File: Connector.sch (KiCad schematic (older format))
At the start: 10 parts, among them CON11 DISCO-CON, CON12 DISCO-CON

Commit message: Resolves Bug in Cubesat Connector Library
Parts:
- removed CON12: DISCO-CON, cubesatFunkmodul:Cubesatconnector, symbol DISCO-CON
- CON11: footprint cubesatFunkmodul:Cubesatconnector -> CubeSat-Bus-1_FTS-CLP
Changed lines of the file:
@@
 $EndComp
 $Comp
-L GND #PWR035
+L GND #PWR37
 U 1 1 59C4523B
 P 2300 4700
-F 0 "#PWR035" H 2300 4450 50  0001 C CNN
+F 0 "#PWR37" H 2300 4450 50  0001 C CNN
 F 1 "GND" H 2300 4550 50  0000 C CNN
 F 2 "" H 2300 4700 50  0001 C CNN
@@
 $EndComp
 $Comp
-L GND #PWR036
+L GND #PWR38
 U 1 1 59C45255
 P 2600 4700
-F 0 "#PWR036" H 2600 4450 50  0001 C CNN
+F 0 "#PWR38" H 2600 4450 50  0001 C CNN
 F 1 "GND" H 2600 4550 50  0000 C CNN
 F 2 "" H 2600 4700 50  0001 C CNN
@@
 $EndComp
 $Comp
-L GND #PWR037
+L GND #PWR39
 U 1 1 59C4526F
 P 2900 4700
-F 0 "#PWR037" H 2900 4450 50  0001 C CNN
+F 0 "#PWR39" H 2900 4450 50  0001 C CNN
 F 1 "GND" H 2900 4550 50  0000 C CNN
 F 2 "" H 2900 4700 50  0001 C CNN
@@
 $EndComp
 $Comp
-L GND #PWR038
+L GND #PWR40
 U 1 1 59C452E4
 P 3400 4700
-F 0 "#PWR038" H 3400 4450 50  0001 C CNN
+F 0 "#PWR40" H 3400 4450 50  0001 C CNN
 F 1 "GND" H 3400 4550 50  0000 C CNN
 F 2 "" H 3400 4700 50  0001 C CNN
@@
 $EndComp
 $Comp
-L GND #PWR039
+L GND #PWR43
 U 1 1 59C452EA
 P 3700 4700
-F 0 "#PWR039" H 3700 4450 50  0001 C CNN
+F 0 "#PWR43" H 3700 4450 50  0001 C CNN
 F 1 "GND" H 3700 4550 50  0000 C CNN
 F 2 "" H 3700 4700 50  0001 C CNN
@@
 $EndComp
 $Comp
-L GND #PWR040
+L GND #PWR44
 U 1 1 59C452F0
 P 4000 4700
-F 0 "#PWR040" H 4000 4450 50  0001 C CNN
+F 0 "#PWR44" H 4000 4450 50  0001 C CNN
 F 1 "GND" H 4000 4550 50  0000 C CNN
 F 2 "" H 4000 4700 50  0001 C CNN
@@
 $EndComp
 $Comp
-L GND #PWR041
+L GND #PWR45
 U 1 1 59C45994
 P 4650 4700
-F 0 "#PWR041" H 4650 4450 50  0001 C CNN
+F 0 "#PWR45" H 4650 4450 50  0001 C CNN
 F 1 "GND" H 4650 4550 50  0000 C CNN
 F 2 "" H 4650 4700 50  0001 C CNN
@@
 ESD Protection
 $Comp
-L GND #PWR042
-U 1 1 59DA7E4B
-P 7550 950
-F 0 "#PWR042" H 7550 700 50  0001 C CNN
-F 1 "GND" H 7550 800 50  0000 C CNN
-F 2 "" H 7550 950 50  0001 C CNN
-F 3 "" H 7550 950 50  0001 C CNN
-	1    7550 950
-	0    -1   -1   0
-$EndComp
-$Comp
-L GND #PWR043
+L GND #PWR47
 U 1 1 59DA7E71
-P 6250 1200
-F 0 "#PWR043" H 6250 950 50  0001 C CNN
-F 1 "GND" H 6250 1050 50  0000 C CNN
-F 2 "" H 6250 1200 50  0001 C CNN
-F 3 "" H 6250 1200 50  0001 C CNN
-	1    6250 1200
-	0    1    1    0
-$EndComp
-$Comp
-L GND #PWR044
+P 7100 1400
+F 0 "#PWR47" H 7100 1150 50  0001 C CNN
+F 1 "GND" H 7100 1250 50  0000 C CNN
+F 2 "" H 7100 1400 50  0001 C CNN
+F 3 "" H 7100 1400 50  0001 C CNN
+	1    7100 1400
+	0    -1   -1   0
+$EndComp
+$Comp
+L GND #PWR48
 U 1 1 59DA7F27
-P 6250 3100
-F 0 "#PWR044" H 6250 2850 50  0001 C CNN
-F 1 "GND" H 6250 2950 50  0000 C CNN
-F 2 "" H 6250 3100 50  0001 C CNN
-F 3 "" H 6250 3100 50  0001 C CNN
-	1    6250 3100
-	0    1    1    0
-$EndComp
-$Comp
-L GND #PWR045
-U 1 1 59DA7F4D
-P 7550 3850
-F 0 "#PWR045" H 7550 3600 50  0001 C CNN
-F 1 "GND" H 7550 3700 50  0000 C CNN
-F 2 "" H 7550 3850 50  0001 C CNN
-F 3 "" H 7550 3850 50  0001 C CNN
-	1    7550 3850
-	0    -1   -1   0
-$EndComp
-$Comp
-L GND #PWR046
+P 7100 4300
+F 0 "#PWR48" H 7100 4050 50  0001 C CNN
+F 1 "GND" H 7100 4150 50  0000 C CNN
+F 2 "" H 7100 4300 50  0001 C CNN
+F 3 "" H 7100 4300 50  0001 C CNN
+	1    7100 4300
+	0    -1   -1   0
+$EndComp
+$Comp
+L GND #PWR41
 U 1 1 59DA801E
 P 3600 1200
-F 0 "#PWR046" H 3600 950 50  0001 C CNN
+F 0 "#PWR41" H 3600 950 50  0001 C CNN
 F 1 "GND" H 3600 1050 50  0000 C CNN
 F 2 "" H 3600 1200 50  0001 C CNN
@@
 $EndComp
 $Comp
-L GND #PWR047
+L GND #PWR35
 U 1 1 59DA8044
 P 2000 1200
-F 0 "#PWR047" H 2000 950 50  0001 C CNN
+F 0 "#PWR35" H 2000 950 50  0001 C CNN
 F 1 "GND" H 2000 1050 50  0000 C CNN
 F 2 "" H 2000 1200 50  0001 C CNN
@@
 $EndComp
 $Comp
-L GND #PWR048
+L GND #PWR36
 U 1 1 59DA8115
 P 2000 3100
-F 0 "#PWR048" H 2000 2850 50  0001 C CNN
+F 0 "#PWR36" H 2000 2850 50  0001 C CNN
 F 1 "GND" H 2000 2950 50  0000 C CNN
 F 2 "" H 2000 3100 50  0001 C CNN
@@
 $EndComp
 $Comp
-L GND #PWR049
+L GND #PWR42
 U 1 1 59DA82BE
 P 3600 3100
-F 0 "#PWR049" H 3600 2850 50  0001 C CNN
+F 0 "#PWR42" H 3600 2850 50  0001 C CNN
 F 1 "GND" H 3600 2950 50  0000 C CNN
 F 2 "" H 3600 3100 50  0001 C CNN
@@
 $EndComp
 $Comp
-L GND #PWR050
+L GND #PWR46
 U 1 1 59DAB906
 P 5100 4650
-F 0 "#PWR050" H 5100 4400 50  0001 C CNN
+F 0 "#PWR46" H 5100 4400 50  0001 C CNN
 F 1 "GND" H 5100 4500 50  0000 C CNN
 F 2 "" H 5100 4650 50  0001 C CNN
@@
 $EndComp
 $Comp
-L DISCO-CON CON12
-U 1 1 59E5D7B1
-P 10400 2250
-F 0 "CON12" H 10100 3780 45  0000 L BNN
-F 1 "DISCO-CON" H 10100 570 45  0000 L BNN
-F 2 "cubesatFunkmodul:Cubesatconnector" H 10430 2400 20  0001 C CNN
-F 3 "" H 10400 2250 60  0001 C CNN
-	1    10400 2250
-	1    0    0    -1
-$EndComp
-$Comp
 L DISCO-CON CON11
-U 1 1 59E5D88F
-P 7050 2350
-F 0 "CON11" H 6750 3880 45  0000 L BNN
-F 1 "DISCO-CON" H 6750 670 45  0000 L BNN
-F 2 "cubesatFunkmodul:Cubesatconnector" H 7080 2500 20  0001 C CNN
-F 3 "" H 7050 2350 60  0001 C CNN
-	1    7050 2350
+U 1 1 59F62198
+P 6600 2800
+F 0 "CON11" H 6300 4330 45  0000 L BNN
+F 1 "DISCO-CON" H 6300 1120 45  0000 L BNN
+F 2 "CubeSat-Bus-1_FTS-CLP" H 6630 2950 20  0001 C CNN
+F 3 "" H 6600 2800 60  0001 C CNN
+	1    6600 2800
 	-1   0    0    -1
 $EndComp

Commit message: Integrates Connectors in Design
Beginn to add mounting holes
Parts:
- removed CON11: DISCO-CON, CubeSat-Bus-1_FTS-CLP, symbol DISCO-CON
- added CON11: DISCO-CON1, cubesatFunkmodul:Cubesatconnector, symbol DISCO-CON1
- added CON21: DISCO-CON2, cubesatFunkmodul:Cubesatconnector, symbol DISCO-CON2
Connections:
- net labels added: TCK, TDI, TDO, TDO-Rf, TMS, ~RBF~
- net labels removed: VBAT
- wire segments 4 -> 1
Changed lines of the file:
@@
 LIBS:nxp-ic
 LIBS:7400-ic
-LIBS:cubesatFunkmodul-cache
 LIBS:funkmodul
 LIBS:CubeSat-Bus-1
 LIBS:CubeSat-Bus-2
+LIBS:disco-con
 EELAYER 25 0
 EELAYER END
@@
 $EndComp
 $Comp
-L GND #PWR37
+L GND #PWR035
 U 1 1 59C4523B
 P 2300 4700
-F 0 "#PWR37" H 2300 4450 50  0001 C CNN
+F 0 "#PWR035" H 2300 4450 50  0001 C CNN
 F 1 "GND" H 2300 4550 50  0000 C CNN
 F 2 "" H 2300 4700 50  0001 C CNN
@@
 $EndComp
 $Comp
-L GND #PWR38
+L GND #PWR036
 U 1 1 59C45255
 P 2600 4700
-F 0 "#PWR38" H 2600 4450 50  0001 C CNN
+F 0 "#PWR036" H 2600 4450 50  0001 C CNN
 F 1 "GND" H 2600 4550 50  0000 C CNN
 F 2 "" H 2600 4700 50  0001 C CNN
@@
 $EndComp
 $Comp
-L GND #PWR39
+L GND #PWR037
 U 1 1 59C4526F
 P 2900 4700
-F 0 "#PWR39" H 2900 4450 50  0001 C CNN
+F 0 "#PWR037" H 2900 4450 50  0001 C CNN
 F 1 "GND" H 2900 4550 50  0000 C CNN
 F 2 "" H 2900 4700 50  0001 C CNN
@@
 $EndComp
 $Comp
-L GND #PWR40
+L GND #PWR038
 U 1 1 59C452E4
 P 3400 4700
-F 0 "#PWR40" H 3400 4450 50  0001 C CNN
+F 0 "#PWR038" H 3400 4450 50  0001 C CNN
 F 1 "GND" H 3400 4550 50  0000 C CNN
 F 2 "" H 3400 4700 50  0001 C CNN
@@
 $EndComp
 $Comp
-L GND #PWR43
+L GND #PWR039
 U 1 1 59C452EA
 P 3700 4700
-F 0 "#PWR43" H 3700 4450 50  0001 C CNN
+F 0 "#PWR039" H 3700 4450 50  0001 C CNN
 F 1 "GND" H 3700 4550 50  0000 C CNN
 F 2 "" H 3700 4700 50  0001 C CNN
@@
 $EndComp
 $Comp
-L GND #PWR44
+L GND #PWR040
 U 1 1 59C452F0
 P 4000 4700
-F 0 "#PWR44" H 4000 4450 50  0001 C CNN
+F 0 "#PWR040" H 4000 4450 50  0001 C CNN
 F 1 "GND" H 4000 4550 50  0000 C CNN
 F 2 "" H 4000 4700 50  0001 C CNN
@@
 $EndComp
 $Comp
-L GND #PWR45
+L GND #PWR041
 U 1 1 59C45994
 P 4650 4700
-F 0 "#PWR45" H 4650 4450 50  0001 C CNN
+F 0 "#PWR041" H 4650 4450 50  0001 C CNN
 F 1 "GND" H 4650 4550 50  0000 C CNN
 F 2 "" H 4650 4700 50  0001 C CNN
@@
 ESD Protection
 $Comp
-L GND #PWR47
+L GND #PWR042
 U 1 1 59DA7E71
 P 7100 1400
-F 0 "#PWR47" H 7100 1150 50  0001 C CNN
+F 0 "#PWR042" H 7100 1150 50  0001 C CNN
 F 1 "GND" H 7100 1250 50  0000 C CNN
 F 2 "" H 7100 1400 50  0001 C CNN
@@
 $EndComp
 $Comp
-L GND #PWR48
+L GND #PWR043
 U 1 1 59DA7F27
 P 7100 4300
-F 0 "#PWR48" H 7100 4050 50  0001 C CNN
+F 0 "#PWR043" H 7100 4050 50  0001 C CNN
 F 1 "GND" H 7100 4150 50  0000 C CNN
 F 2 "" H 7100 4300 50  0001 C CNN
@@
 	0    -1   -1   0
 $EndComp
-$Comp
-L GND #PWR41
-U 1 1 59DA801E
-P 3600 1200
-F 0 "#PWR41" H 3600 950 50  0001 C CNN
-F 1 "GND" H 3600 1050 50  0000 C CNN
-F 2 "" H 3600 1200 50  0001 C CNN
-F 3 "" H 3600 1200 50  0001 C CNN
-	1    3600 1200
-	0    -1   -1   0
-$EndComp
-$Comp
-L GND #PWR35
-U 1 1 59DA8044
-P 2000 1200
-F 0 "#PWR35" H 2000 950 50  0001 C CNN
-F 1 "GND" H 2000 1050 50  0000 C CNN
-F 2 "" H 2000 1200 50  0001 C CNN
-F 3 "" H 2000 1200 50  0001 C CNN
-	1    2000 1200
-	0    1    1    0
-$EndComp
-$Comp
-L GND #PWR36
-U 1 1 59DA8115
-P 2000 3100
-F 0 "#PWR36" H 2000 2850 50  0001 C CNN
-F 1 "GND" H 2000 2950 50  0000 C CNN
-F 2 "" H 2000 3100 50  0001 C CNN
-F 3 "" H 2000 3100 50  0001 C CNN
-	1    2000 3100
-	0    1    1    0
-$EndComp
-$Comp
-L GND #PWR42
-U 1 1 59DA82BE
-P 3600 3100
-F 0 "#PWR42" H 3600 2850 50  0001 C CNN
-F 1 "GND" H 3600 2950 50  0000 C CNN
-F 2 "" H 3600 3100 50  0001 C CNN
-F 3 "" H 3600 3100 50  0001 C CNN
-	1    3600 3100
-	0    -1   -1   0
-$EndComp
-Text HLabel 1650 1400 0    60   Input ~ 0
+Text HLabel 7100 2100 2    60   Input ~ 0
 3.3V
-Text HLabel 3850 1400 2    60   Input ~ 0
-3.3V
-Wire Wire Line
-	1650 1400 2000 1400
-Wire Wire Line
-	3600 1400 3850 1400
-Text GLabel 1650 1300 0    60   Input ~ 0
-VBAT
-Text GLabel 3900 1300 2    60   Input ~ 0
-VBAT
-Wire Wire Line
-	3600 1300 3900 1300
-Wire Wire Line
-	1650 1300 2000 1300
-Text HLabel 6250 2200 0    60   Input ~ 0
+Text HLabel 7100 3500 2    60   Input ~ 0
 TX1
-Text HLabel 6250 2300 0    60   Input ~ 0
+Text HLabel 7100 3600 2    60   Input ~ 0
 RX1
-Text HLabel 7850 2200 2    60   Input ~ 0
+Text HLabel 9450 2900 0    60   Input ~ 0
 TX2
-Text HLabel 7850 2300 2    60   Input ~ 0
+Text HLabel 9450 2800 0    60   Input ~ 0
 RX2
-Text HLabel 6250 1900 0    60   Input ~ 0
-BAT_OK
-Text HLabel 7850 1900 2    60   Input ~ 0
-BAT_OK
 Text HLabel 5100 4350 1    60   Input ~ 0
 BAT_OK
@@
 $EndComp
 $Comp
-L GND #PWR46
+L GND #PWR044
 U 1 1 59DAB906
 P 5100 4650
-F 0 "#PWR46" H 5100 4400 50  0001 C CNN
+F 0 "#PWR044" H 5100 4400 50  0001 C CNN
 F 1 "GND" H 5100 4500 50  0000 C CNN
 F 2 "" H 5100 4650 50  0001 C CNN
@@
 $EndComp
 $Comp
-L DISCO-CON CON11
-U 1 1 59F62198
+L DISCO-CON2 CON21
+U 1 1 59FBB064
+P 9950 2700
+F 0 "CON21" H 9650 4230 45  0000 L BNN
+F 1 "DISCO-CON2" H 9650 1020 45  0000 L BNN
+F 2 "cubesatFunkmodul:Cubesatconnector" H 9980 2850 20  0001 C CNN
+F 3 "" H 9950 2700 60  0001 C CNN
+	1    9950 2700
+	1    0    0    -1
+$EndComp
+$Comp
+L DISCO-CON1 CON11
+U 1 1 59FBB0E1
 P 6600 2800
 F 0 "CON11" H 6300 4330 45  0000 L BNN
-F 1 "DISCO-CON" H 6300 1120 45  0000 L BNN
-F 2 "CubeSat-Bus-1_FTS-CLP" H 6630 2950 20  0001 C CNN
+F 1 "DISCO-CON1" H 6300 1120 45  0000 L BNN
+F 2 "cubesatFunkmodul:Cubesatconnector" H 6630 2950 20  0001 C CNN
 F 3 "" H 6600 2800 60  0001 C CNN
 	1    6600 2800
 	-1   0    0    -1
 $EndComp
+Text HLabel 9450 2500 0    60   Input ~ 0
+BAT_OK
+Text HLabel 9450 1400 0    60   Input ~ 0
+TCK
+Text HLabel 9450 1500 0    60   Input ~ 0
+TMS
+Text HLabel 9450 1600 0    60   Input ~ 0
+TDI
+Text HLabel 9450 1700 0    60   Input ~ 0
+TDO
+Text HLabel 9450 1800 0    60   Input ~ 0
+TDO-Rf
+Text HLabel 7100 3400 2    60   Input ~ 0
+~ENABLE1~
+Text HLabel 9450 3000 0    60   Input ~ 0
+~ENABLE2~
+Text HLabel 9450 3500 0    60   Input ~ 0
+~RBF~
+$Comp
+L GND #PWR045
+U 1 1 59FBC03F
+P 9450 1300
+F 0 "#PWR045" H 9450 1050 50  0001 C CNN
+F 1 "GND" H 9450 1150 50  0000 C CNN
+F 2 "" H 9450 1300 50  0001 C CNN
+F 3 "" H 9450 1300 50  0001 C CNN
+	1    9450 1300
+	0    1    1    0
+$EndComp
+$Comp
+L GND #PWR046
+U 1 1 59FBC107
+P 9450 4300
+F 0 "#PWR046" H 9450 4050 50  0001 C CNN
+F 1 "GND" H 9450 4150 50  0000 C CNN
+F 2 "" H 9450 4300 50  0001 C CNN
+F 3 "" H 9450 4300 50  0001 C CNN
+	1    9450 4300
+	1    0    0    -1
+$EndComp
+Wire Wire Line
+	9450 4100 9450 4300
+Connection ~ 9450 4200
 $EndSCHEMATC

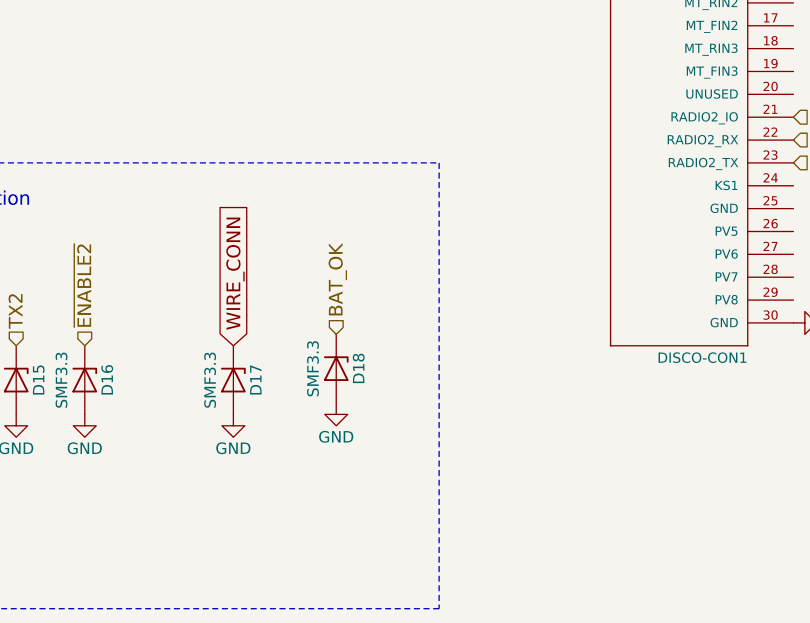
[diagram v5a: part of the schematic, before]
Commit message: Adds second burnwire fets
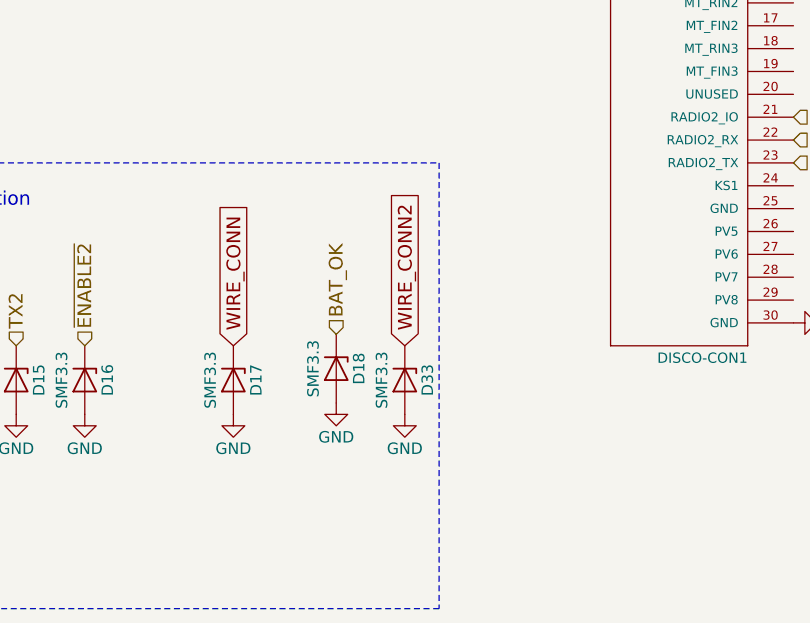
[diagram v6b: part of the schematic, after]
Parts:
- added D33: SMF3.3, Diodes_SMD:D_SOD-123F, symbol D_Zener
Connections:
- net GND: now also D33.2 (A)
- new net WIRE_CONN2: D33.1 (K)
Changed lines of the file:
@@
 $EndComp
 $Comp
-L GND #PWR38
+L GND #PWR038
 U 1 1 59C4523B
 P 2300 4700
-F 0 "#PWR38" H 2300 4450 50  0001 C CNN
+F 0 "#PWR038" H 2300 4450 50  0001 C CNN
 F 1 "GND" H 2300 4550 50  0000 C CNN
 F 2 "" H 2300 4700 50  0001 C CNN
@@
 $EndComp
 $Comp
-L GND #PWR39
+L GND #PWR039
 U 1 1 59C45255
 P 2600 4700
-F 0 "#PWR39" H 2600 4450 50  0001 C CNN
+F 0 "#PWR039" H 2600 4450 50  0001 C CNN
 F 1 "GND" H 2600 4550 50  0000 C CNN
 F 2 "" H 2600 4700 50  0001 C CNN
@@
 $EndComp
 $Comp
-L GND #PWR40
+L GND #PWR040
 U 1 1 59C4526F
 P 2900 4700
-F 0 "#PWR40" H 2900 4450 50  0001 C CNN
+F 0 "#PWR040" H 2900 4450 50  0001 C CNN
 F 1 "GND" H 2900 4550 50  0000 C CNN
 F 2 "" H 2900 4700 50  0001 C CNN
@@
 $EndComp
 $Comp
-L GND #PWR41
+L GND #PWR041
 U 1 1 59C452E4
 P 3400 4700
-F 0 "#PWR41" H 3400 4450 50  0001 C CNN
+F 0 "#PWR041" H 3400 4450 50  0001 C CNN
 F 1 "GND" H 3400 4550 50  0000 C CNN
 F 2 "" H 3400 4700 50  0001 C CNN
@@
 $EndComp
 $Comp
-L GND #PWR42
+L GND #PWR042
 U 1 1 59C452EA
 P 3700 4700
-F 0 "#PWR42" H 3700 4450 50  0001 C CNN
+F 0 "#PWR042" H 3700 4450 50  0001 C CNN
 F 1 "GND" H 3700 4550 50  0000 C CNN
 F 2 "" H 3700 4700 50  0001 C CNN
@@
 $EndComp
 $Comp
-L GND #PWR43
+L GND #PWR043
 U 1 1 59C452F0
 P 4000 4700
-F 0 "#PWR43" H 4000 4450 50  0001 C CNN
+F 0 "#PWR043" H 4000 4450 50  0001 C CNN
 F 1 "GND" H 4000 4550 50  0000 C CNN
 F 2 "" H 4000 4700 50  0001 C CNN
@@
 $EndComp
 $Comp
-L GND #PWR44
+L GND #PWR044
 U 1 1 59C45994
 P 4650 4700
-F 0 "#PWR44" H 4650 4450 50  0001 C CNN
+F 0 "#PWR044" H 4650 4450 50  0001 C CNN
 F 1 "GND" H 4650 4550 50  0000 C CNN
 F 2 "" H 4650 4700 50  0001 C CNN
@@
 ESD Protection
 $Comp
-L GND #PWR46
+L GND #PWR045
 U 1 1 59DA7E71
 P 7100 1400
-F 0 "#PWR46" H 7100 1150 50  0001 C CNN
+F 0 "#PWR045" H 7100 1150 50  0001 C CNN
 F 1 "GND" H 7100 1250 50  0000 C CNN
 F 2 "" H 7100 1400 50  0001 C CNN
@@
 $EndComp
 $Comp
-L GND #PWR47
+L GND #PWR046
 U 1 1 59DA7F27
 P 7100 4300
-F 0 "#PWR47" H 7100 4050 50  0001 C CNN
+F 0 "#PWR046" H 7100 4050 50  0001 C CNN
 F 1 "GND" H 7100 4150 50  0000 C CNN
 F 2 "" H 7100 4300 50  0001 C CNN
@@
 $EndComp
 $Comp
-L GND #PWR45
+L GND #PWR047
 U 1 1 59DAB906
 P 5100 4650
-F 0 "#PWR45" H 5100 4400 50  0001 C CNN
+F 0 "#PWR047" H 5100 4400 50  0001 C CNN
 F 1 "GND" H 5100 4500 50  0000 C CNN
 F 2 "" H 5100 4650 50  0001 C CNN
@@
 ~RBF~
 $Comp
-L GND #PWR48
+L GND #PWR048
 U 1 1 59FBC03F
 P 9450 1300
-F 0 "#PWR48" H 9450 1050 50  0001 C CNN
+F 0 "#PWR048" H 9450 1050 50  0001 C CNN
 F 1 "GND" H 9450 1150 50  0000 C CNN
 F 2 "" H 9450 1300 50  0001 C CNN
@@
 $EndComp
 $Comp
-L GND #PWR49
+L GND #PWR049
 U 1 1 59FBC107
 P 9450 4300
-F 0 "#PWR49" H 9450 4050 50  0001 C CNN
+F 0 "#PWR049" H 9450 4050 50  0001 C CNN
 F 1 "GND" H 9450 4150 50  0000 C CNN
 F 2 "" H 9450 4300 50  0001 C CNN
@@
 	9450 4100 9450 4300
 Connection ~ 9450 4200
+Text GLabel 5400 4400 1    60   Input ~ 0
+WIRE_CONN2
+$Comp
+L D_Zener D33
+U 1 1 5A0B499B
+P 5400 4550
+F 0 "D33" H 5400 4650 50  0000 C CNN
+F 1 "SMF3.3" H 5400 4450 50  0000 C CNN
+F 2 "Diodes_SMD:D_SOD-123F" H 5400 4550 50  0001 C CNN
+F 3 "" H 5400 4550 50  0001 C CNN
+	1    5400 4550
+	0    1    1    0
+$EndComp
+$Comp
+L GND #PWR050
+U 1 1 5A0B49A1
+P 5400 4700
+F 0 "#PWR050" H 5400 4450 50  0001 C CNN
+F 1 "GND" H 5400 4550 50  0000 C CNN
+F 2 "" H 5400 4700 50  0001 C CNN
+F 3 "" H 5400 4700 50  0001 C CNN
+	1    5400 4700
+	1    0    0    -1
+$EndComp
 $EndSCHEMATC
